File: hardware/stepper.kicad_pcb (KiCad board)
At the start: 4 copper layers, 40 x 40 mm, 128 parts, among them J101 USB-MINI-B-SMD, J102 DRILL, J103 DRILL, J104 DRILL, J105 DRILL, J401 STACK-UP-HIGH, J402 STACK-DOWN, J403 STACK-UP-HIGH, J404 STACK-DOWN, P201 black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

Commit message: change clock series resistor 1k->470
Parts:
- C210, C212, C214, C216: value DNP -> 470pF/100V
- R105: value 1k -> 470
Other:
- board text added: "Very near!"
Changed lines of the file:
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@@
     (links 410)
     (no_connects 2)
-    (area 126.671069 72.726549 166.772591 112.825531)
+    (area 125.845139 71.945139 283.420502 165.440043)
     (thickness 1.6002)
-    (drawings 63)
+    (drawings 64)
     (tracks 2660)
     (zones 0)
@@
     (aux_axis_origin 126.72568 112.776)
     (grid_origin 148.925 96.65)
-    (visible_elements FFFF5FBF)
+    (visible_elements FFFF5FFF)
     (pcbplotparams
       (layerselection 0x010fc_80000007)
@@
       (effects (font (size 0.2 0.2) (thickness 0.05)))
     )
-    (fp_text value DNP (at 0.05 -0.375 180) (layer F.SilkS)
+    (fp_text value 470pF/100V (at 0.05 -0.375 180) (layer F.SilkS)
       (effects (font (size 0.2 0.2) (thickness 0.05)))
     )
@@
       (effects (font (size 0.2 0.2) (thickness 0.05)))
     )
-    (fp_text value DNP (at 0.05 -0.375) (layer F.SilkS)
+    (fp_text value 470pF/100V (at 0.05 -0.375) (layer F.SilkS)
       (effects (font (size 0.2 0.2) (thickness 0.05)))
     )
@@
       (effects (font (size 0.2 0.2) (thickness 0.05)))
     )
-    (fp_text value DNP (at 0.05 -0.375 180) (layer F.SilkS)
+    (fp_text value 470pF/100V (at 0.05 -0.375 180) (layer F.SilkS)
       (effects (font (size 0.2 0.2) (thickness 0.05)))
     )
@@
       (effects (font (size 0.2 0.2) (thickness 0.05)))
     )
-    (fp_text value DNP (at 0.05 -0.375) (layer F.SilkS)
+    (fp_text value 470pF/100V (at 0.05 -0.375) (layer F.SilkS)
       (effects (font (size 0.2 0.2) (thickness 0.05)))
     )
@@
       (effects (font (size 0.2 0.2) (thickness 0.05)))
     )
-    (fp_text value 1k (at 0 -0.275) (layer F.SilkS)
+    (fp_text value 470 (at 0 -0.275) (layer F.SilkS)
       (effects (font (size 0.2 0.2) (thickness 0.05)))
     )
@@
       (effects (font (size 0.3 0.3) (thickness 0.075)))
     )
-    (fp_text value 82400152 (at 0 0 180) (layer F.SilkS)
+    (fp_text value 82400152 (at -0.325 -0.1 180) (layer F.SilkS)
       (effects (font (size 0.29972 0.29972) (thickness 0.0762)))
     )
@@
       (net 101 "Net-(L101-Pad3)") (clearance 0.14986))
   )
+  (gr_text "Very near!" (at 155.475 98.85) (layer F.SilkS)
+    (effects (font (size 0.29972 0.29972) (thickness 0.07493)))
+  )
   (gr_text "Silent\nStepper\n1.0" (at 163.8 103.85) (layer F.SilkS)

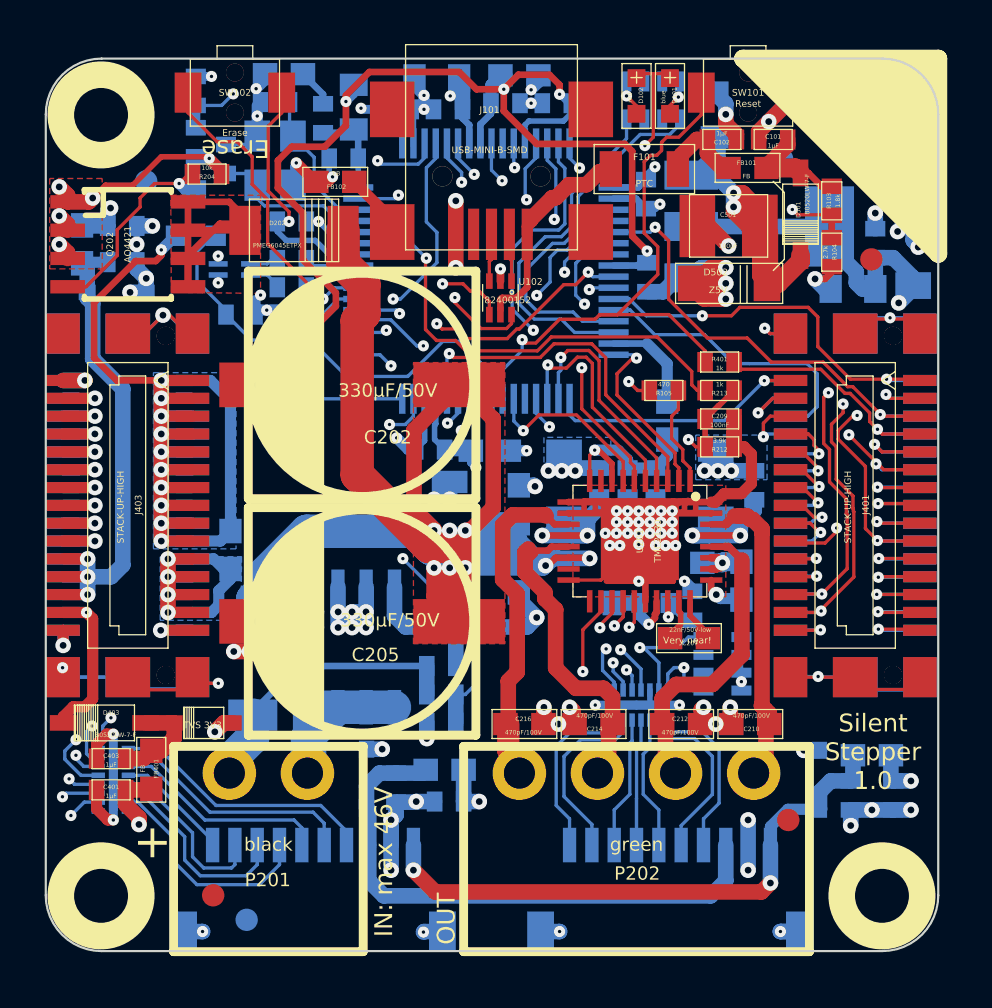
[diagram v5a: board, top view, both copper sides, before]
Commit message: swap pins, add series resistors, add clock pi filter
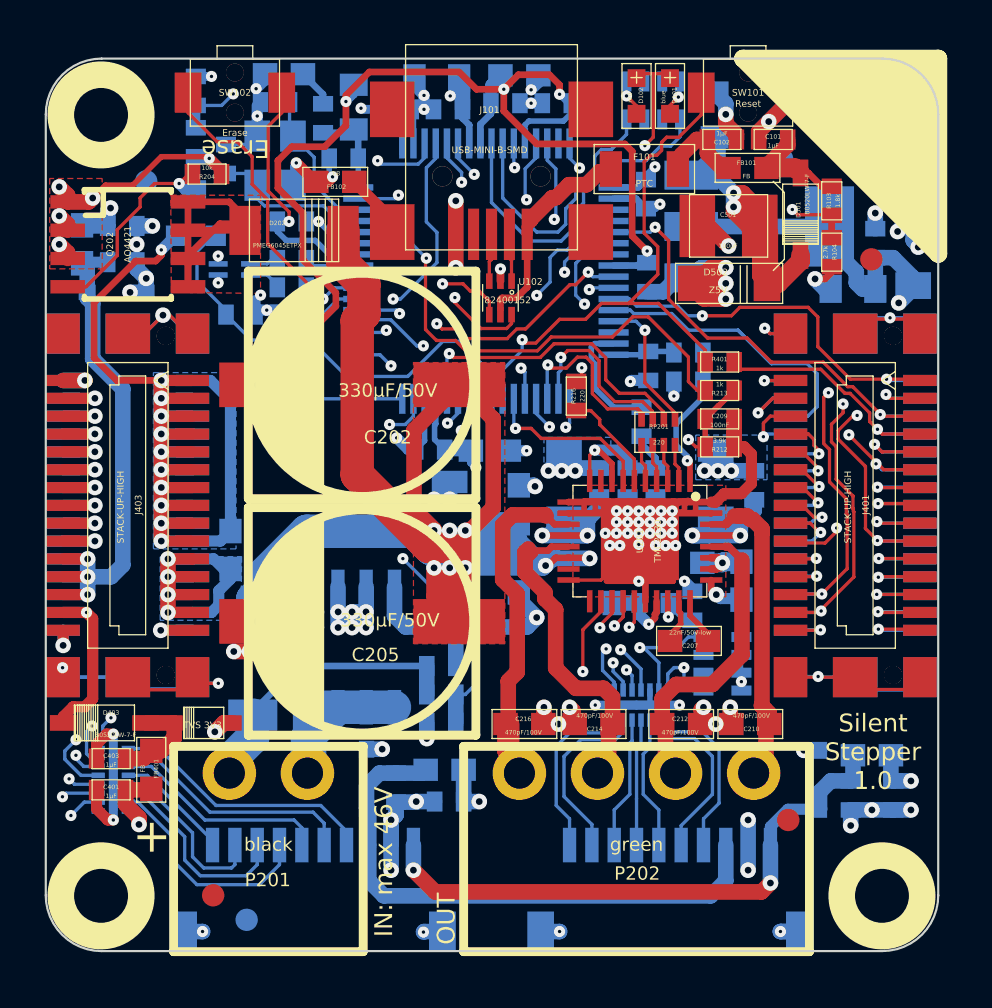
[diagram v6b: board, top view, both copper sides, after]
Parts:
- added C105: 5pF, kicad-libraries:0402E, B.Cu at (153.7, 86.5)
- added C106: 5pF, kicad-libraries:0402E, B.Cu at (155.5, 87.2)
- added R216: 220, kicad-libraries:0402E, F.Cu at (150.5, 87.9)
- added RP201: 220, kicad-libraries:4X0402, F.Cu at (154.2, 89.5)
- R105: value 470 -> 100; moved to B.Cu
- R209: footprint kicad-libraries:0603E -> kicad-libraries:0402E
- moved R105 2.02 mm to (155.5, 86.0)
- moved R209 1.15 mm to (153.4, 89.0)
- moved C207 0.12 mm to (155.6, 98.9)
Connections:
- R105 pad 1: Net-(R105-Pad1) -> Net-(C105-Pad1)
- U101 pad 10: (no net) -> Net-(RP101-Pad5)
- U101 pad 15: PWR-ENABLE -> (no net)
- U101 pad 29: Net-(RP101-Pad8) -> PWR-CS
- U101 pad 30: Net-(RP101-Pad5) -> (no net)
- U101 pad 32: PWR-CS -> Net-(C105-Pad1)
- U101 pad 37: (no net) -> PWR-ENABLE
- U101 pad 9: Net-(R105-Pad1) -> Net-(RP101-Pad8)
- U201 pad 2: PWR-CS -> Net-(RP201-Pad8)
- U201 pad 3: PWR-SCK -> Net-(RP201-Pad7)
- U201 pad 4: PWR-SDI -> Net-(RP201-Pad6)
- U201 pad 5: PWR-SDO -> Net-(RP201-Pad5)
- U201 pad 6: PWR-STEP -> Net-(R216-Pad2)
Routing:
- net Net-(R105-Pad1): track 15.7 -> 0.00 mm, vias 2 -> 0
- net PWR-ENABLE: track 32.0 -> 20.9 mm
- net PWR-STEP: track 14.2 -> 8.90 mm
- net Net-(R216-Pad2): track 0.00 -> 4.61 mm
- net Net-(RP101-Pad5): track 15.5 -> 12.1 mm
- net Net-(C105-Pad1): track 0.00 -> 3.07 mm
- net STACK-INT: track 40.5 -> 37.6 mm
- net 3V3: track 179.4 -> 182.3 mm
- net STACK-SER-RXD: track 37.4 -> 34.7 mm
- net PWR-SCK: track 16.3 -> 14.1 mm
- net PWR-SDI: track 10.4 -> 8.19 mm
- net PWR-CLK: track 4.52 -> 6.71 mm, vias 0 -> 1
- net PWR-CS: track 8.21 -> 6.02 mm
- net PWR-SDO: track 10.2 -> 8.02 mm
- net STACK-SPI-SELECT: track 13.2 -> 15.3 mm
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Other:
- board text removed: "Very near!"
